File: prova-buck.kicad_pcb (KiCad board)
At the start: 2 copper layers, 53 x 40 mm, 44 parts, among them J1 Screw_Terminal_01x02, J2 Barrel_Jack_MountingPin, J3 USB_B_Micro, J4 Conn_02x03_Odd_Even, J5 Conn_02x03_Odd_Even, J6 Conn_01x04, J7 Conn_01x04, J8 Conn_01x02, J9 Conn_01x02, Q1 AO3401A, Q2 AO3401A, U1 MPQ9842GL, U2 LDL1117S33R, U3 LM358

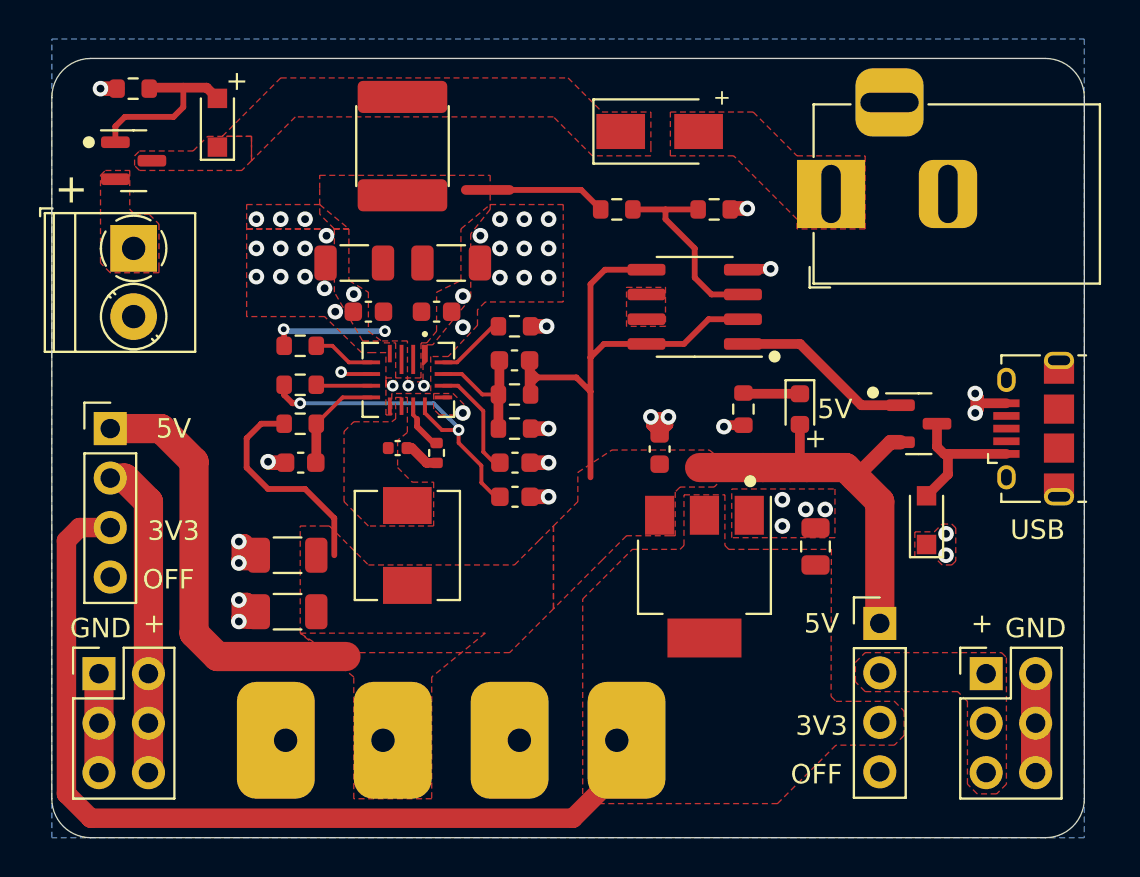
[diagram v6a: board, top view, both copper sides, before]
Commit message: Added .gitignore
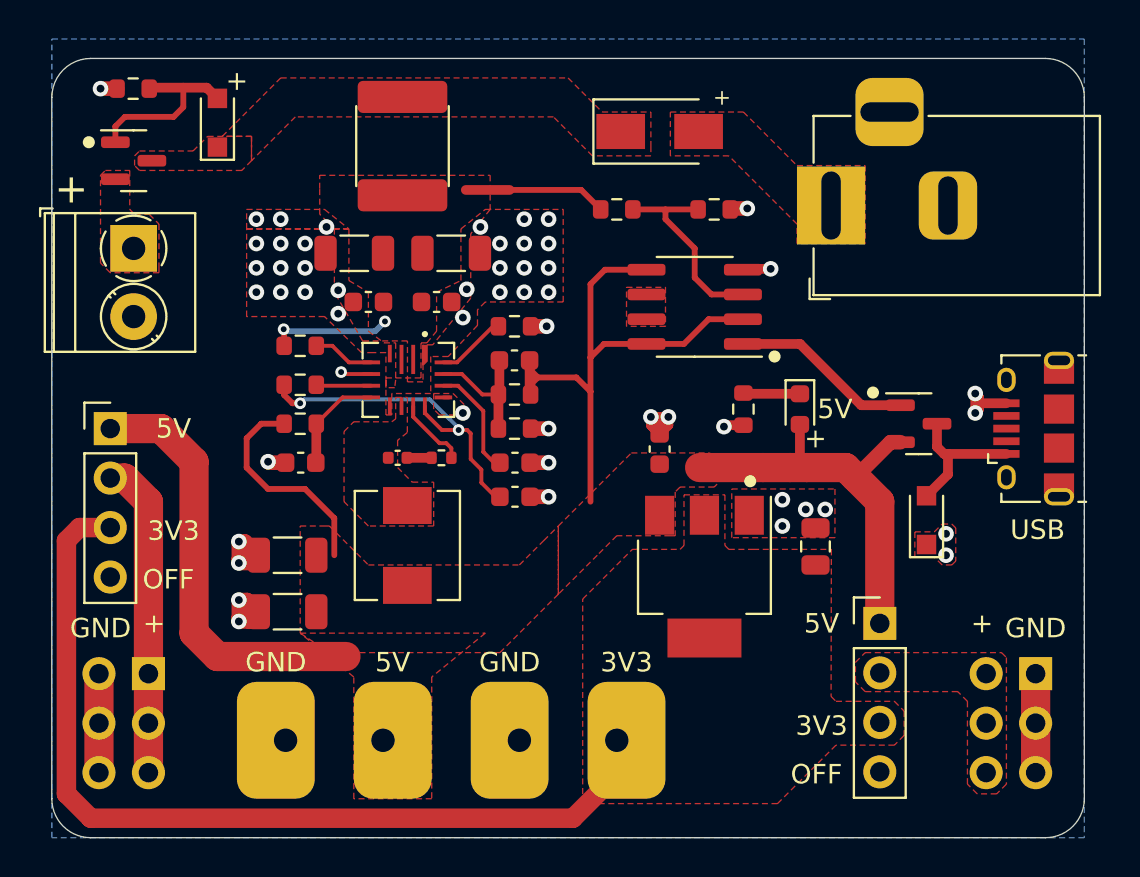
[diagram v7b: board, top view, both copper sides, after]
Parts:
- J4, J5: moved to B.Cu
- moved J4 2.54 mm to (167.5, 106.6), turned to 180 degrees
- moved J5 2.54 mm to (122.0, 106.6), turned to 180 degrees
- moved J2 0.59 mm to (157.0, 82.5)
- moved C1 0.50 mm to (132.5, 85.0)
- moved C2 0.50 mm to (137.5, 85.0)
- moved C4 0.50 mm to (136.8, 87.5)
- moved C5 0.50 mm to (133.2, 87.5)
- moved C6 0.50 mm to (134.8, 95.5)
- moved R8 0.35 mm to (137.0, 95.5), turned to 180 degrees
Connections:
- J4 pad 1: Vleft -> GND
- J4 pad 2: GND -> Vleft
- J4 pad 3: Vleft -> GND
- J4 pad 4: GND -> Vleft
- J4 pad 5: Vleft -> GND
- J4 pad 6: GND -> Vleft
- J5 pad 1: GND -> Vright
- J5 pad 2: Vright -> GND
- J5 pad 3: GND -> Vright
- J5 pad 4: Vright -> GND
- J5 pad 5: GND -> Vright
- J5 pad 6: Vright -> GND
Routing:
- net +5V: track 84.1 -> 85.3 mm
- net /BST: track 2.48 -> 3.67 mm
- net /Rboost: track 1.83 -> 1.26 mm

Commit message: "Generated gerbers"
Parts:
- added G***: LOGO, Symbol:github, B.Cu at (140.8, 81.5)
- added G***: LOGO, Symbol:qrcode-19.8mm, B.Cu at (140.8, 95.9)
- added REF**: JLCPCB-ASSEMBLY-toolinghole, MountingHole:JLCPCB-ASSEMBLY-toolinghole, F.Cu at (162.2, 111.8)
- added REF**: JLCPCB-ASSEMBLY-toolinghole, MountingHole:JLCPCB-ASSEMBLY-toolinghole, F.Cu at (124.6, 111.7)
- added REF**: JLCPCB-ASSEMBLY-toolinghole, MountingHole:JLCPCB-ASSEMBLY-toolinghole, F.Cu at (167.8, 79.1)
- moved C3 0.25 mm to (140.8, 97.8)
- moved J3 0.20 mm to (167.2, 94.0)
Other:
- rule pad_to_mask_clearance: 0 -> 0.05
- board text added: "JLCJLCJLCJLC"
